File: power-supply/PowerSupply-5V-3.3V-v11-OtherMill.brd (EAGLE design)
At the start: 31.8 x 31.8 mm, 19 parts, among them J1 POWER_JACK, J3 VCC, J4 GND, J5 NC1, J6 NC2, U1 LM317

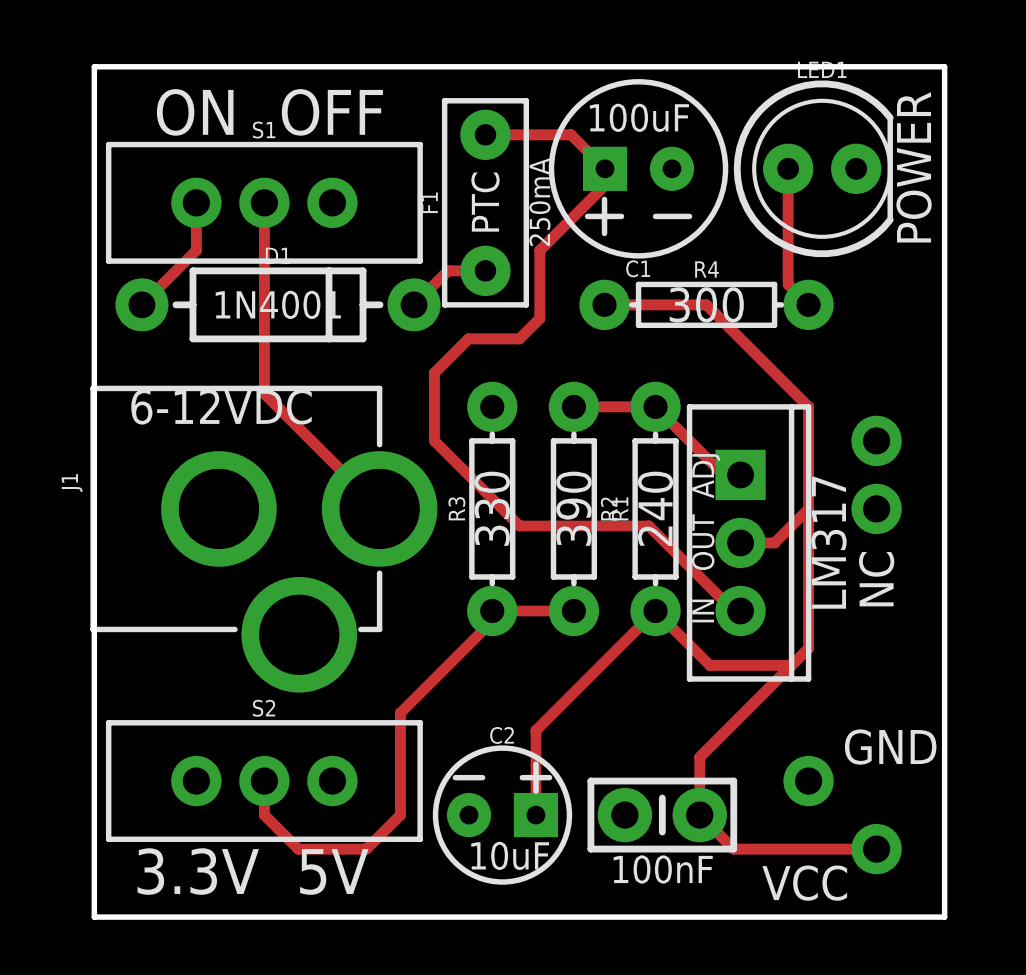
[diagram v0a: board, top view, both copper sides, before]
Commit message: Add raw voltage source
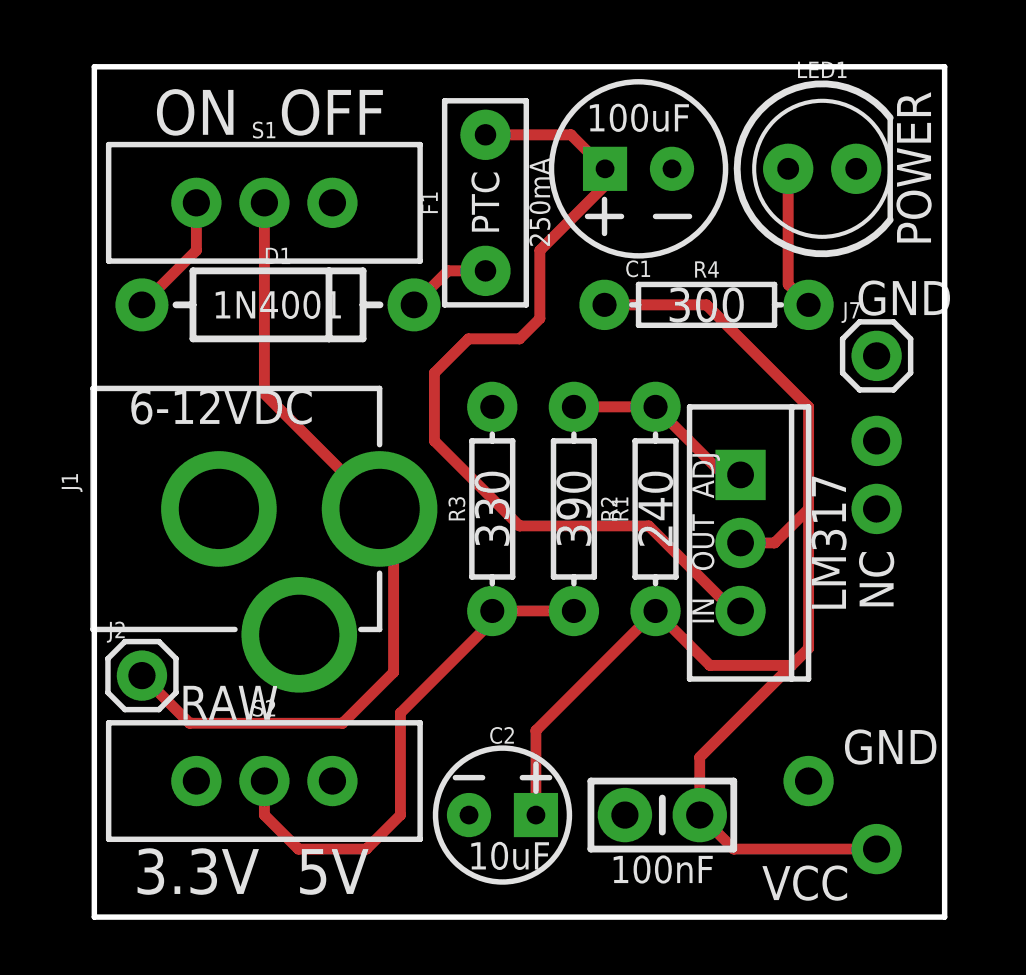
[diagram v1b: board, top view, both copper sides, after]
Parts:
- added J2: RAW, SparkFun-Connectors:1X01
- added J7: GND, SparkFun-Connectors:1X01
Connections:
- net GND: now also J7.1
- net VIN: now also J2.1
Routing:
- net VIN: track 13.2 -> 31.4 mm
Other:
- board text added: "RAW"
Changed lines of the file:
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@@
 <text x="22.733" y="11.43" size="0.8128" layer="21" font="vector" ratio="12" rot="R270" align="center">IN</text>
 <text x="27.432" y="13.97" size="1.27" layer="21" font="vector" ratio="12" rot="R270" align="center">LM317</text>
+<text x="3.175" y="7.366" size="1.27" layer="21" font="vector">RAW</text>
+<text x="28.448" y="22.479" size="1.27" layer="21" font="vector">GND</text>
 </plain>
 <attributes>
@@
 <element name="J5" library="SparkFun-Connectors" package="1X01" value="NC1" x="29.21" y="15.24" rot="MR90"/>
 <element name="J6" library="SparkFun-Connectors" package="1X01" value="NC2" x="29.21" y="17.78" rot="MR90"/>
+<element name="J2" library="SparkFun-Connectors" package="1X01" value="RAW" x="1.778" y="9.017"/>
+<element name="J7" library="SparkFun-Connectors" package="1X01" value="GND" x="29.21" y="20.955"/>
 </elements>
 <signals>
@@
 <contactref element="J1" pad="PWR"/>
 <contactref element="S1" pad="2"/>
-<wire x1="10.652" y1="15.24" x2="6.35" y2="19.542" width="0.4064" layer="1"/>
+<wire x1="6.35" y1="19.542" x2="10.652" y2="15.24" width="0.4064" layer="1"/>
 <wire x1="6.35" y1="19.542" x2="6.35" y2="26.67" width="0.4064" layer="1"/>
+<contactref element="J2" pad="1"/>
+<wire x1="10.652" y1="15.24" x2="11.303" y2="14.589" width="0.4064" layer="1"/>
+<wire x1="3.556" y1="7.239" x2="1.778" y2="9.017" width="0.4064" layer="1"/>
+<wire x1="10.652" y1="15.24" x2="11.176" y2="14.716" width="0.4064" layer="1"/>
+<wire x1="11.176" y1="14.716" x2="11.176" y2="9.144" width="0.4064" layer="1"/>
+<wire x1="11.176" y1="9.144" x2="9.271" y2="7.239" width="0.4064" layer="1"/>
+<wire x1="9.271" y1="7.239" x2="3.556" y2="7.239" width="0.4064" layer="1"/>
 </signal>
 <signal name="GND">
@@
 <vertex x="0" y="0"/>
 </polygon>
+<contactref element="J7" pad="1"/>
 </signal>
 <signal name="ON">

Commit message: Make major bottom layer (see description)
Since OtherMill just mills the board but doesn't pour copper over the
holes. The top and the bottom layer of a vias are disconnected. In order
to reduce the hard word in soldering, I brough all traces to the bottom
layer & set copper pour for both sides of the board.
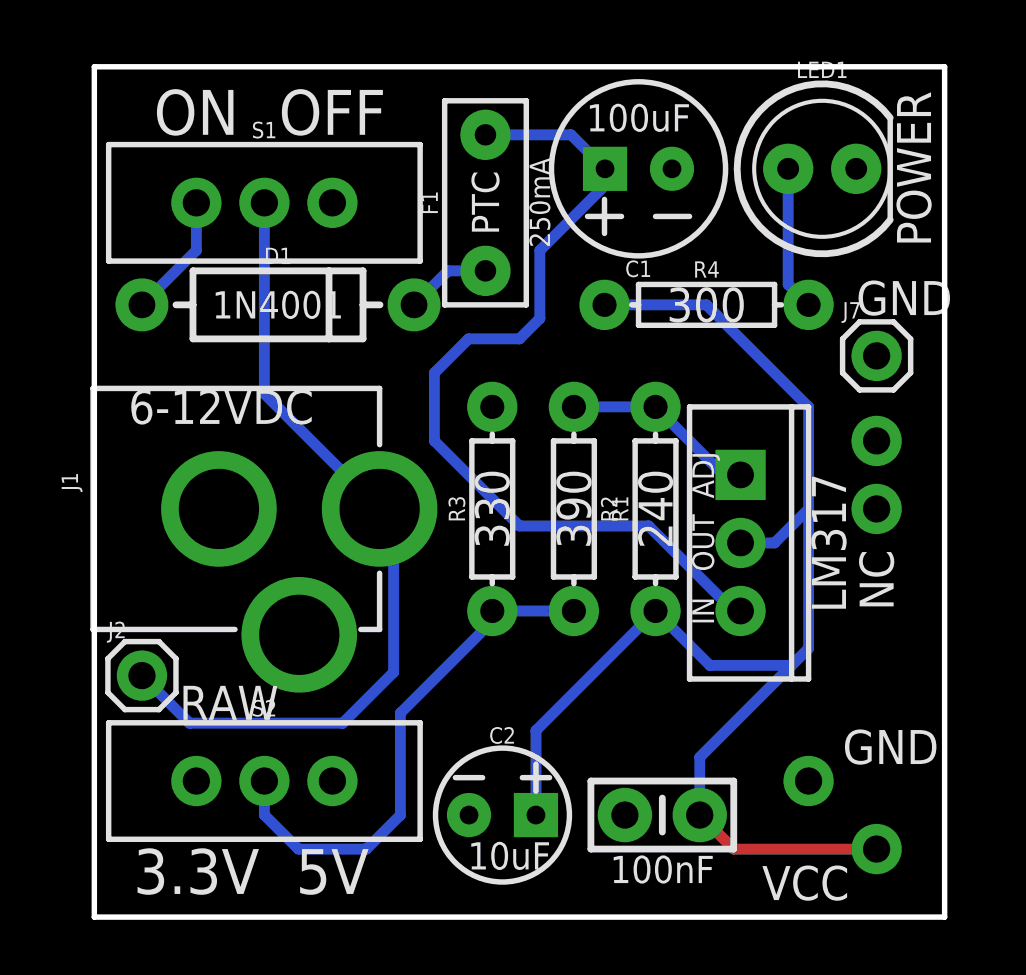
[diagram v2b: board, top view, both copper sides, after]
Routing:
- net VIN: track 31.4 -> 30.6 mm
- added copper zone on layer 1, net GND
